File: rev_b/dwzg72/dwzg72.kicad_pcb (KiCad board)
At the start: 2 copper layers, 285 x 94.6 mm, 305 parts, among them J1 USB_B_Micro, J2 ISP, Q1 FDS9926A, SW1 circumflex, SW10 nine, SW11 zero, SW12 eszett, SW13 accent, SW14 backspace, SW15 pos1, SW16 tab, SW17 q, SW18 w, SW19 e, SW2 one, SW20 r, SW21 t, SW22 z, SW23 u, SW24 i, SW25 o, SW26 p, SW27 ü, SW28 plus, SW29 end, SW3 two, SW30 escape, SW31 a, SW32 s, SW33 d, SW34 f, SW35 g, SW36 h, SW37 j, SW38 k, SW39 l, SW4 three, SW40 ö, SW41 ä, SW42 hash, SW43 enter, SW44 delete, SW45 lshift, SW46 smaller, SW47 y, SW48 x, SW49 c, SW5 four, SW50 v, SW51 b, SW52 n, SW53 m, SW54 comma, SW55 dot, SW56 dash, SW57 up, SW58 rshift, SW59 pageup, SW6 five, SW60 control, SW61 super, SW62 alt, SW63 func, SW64 lspace, SW65 rspace, SW66 altgr, SW67 super, SW68 control, SW69 left, SW7 six, SW70 down, SW71 right, SW72 pagedown, SW73 RESET, SW8 seven, SW9 eight, U1 ATmega32U4-MU, Y1 16MHz

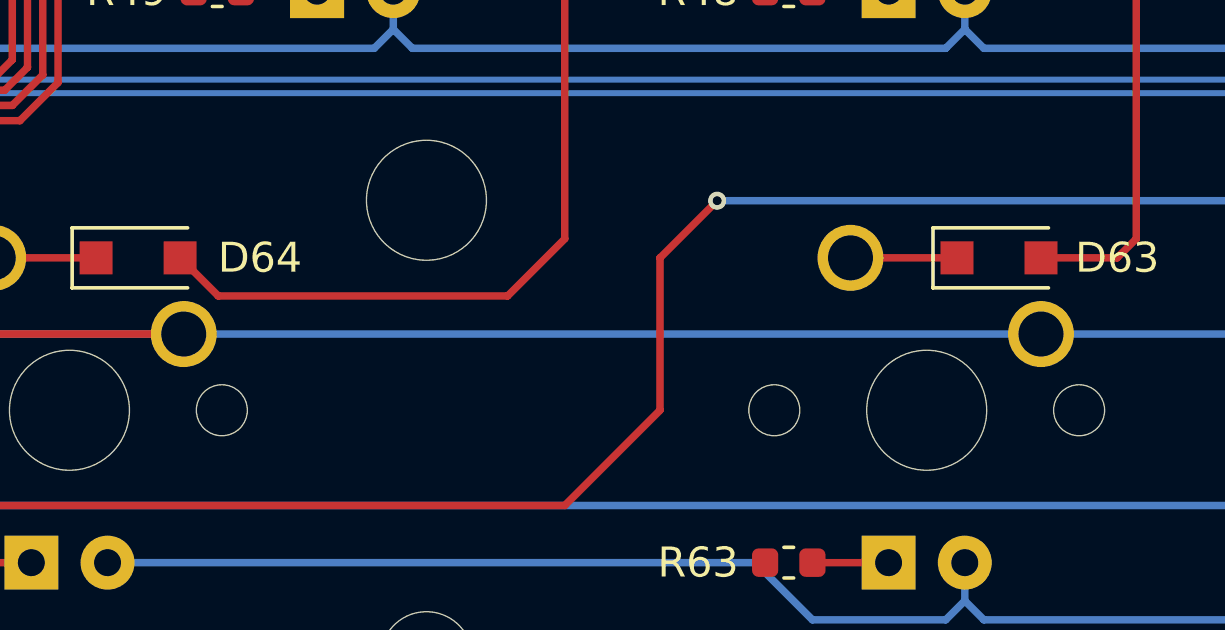
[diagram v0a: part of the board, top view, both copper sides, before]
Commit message: Add logo and revision on PCB
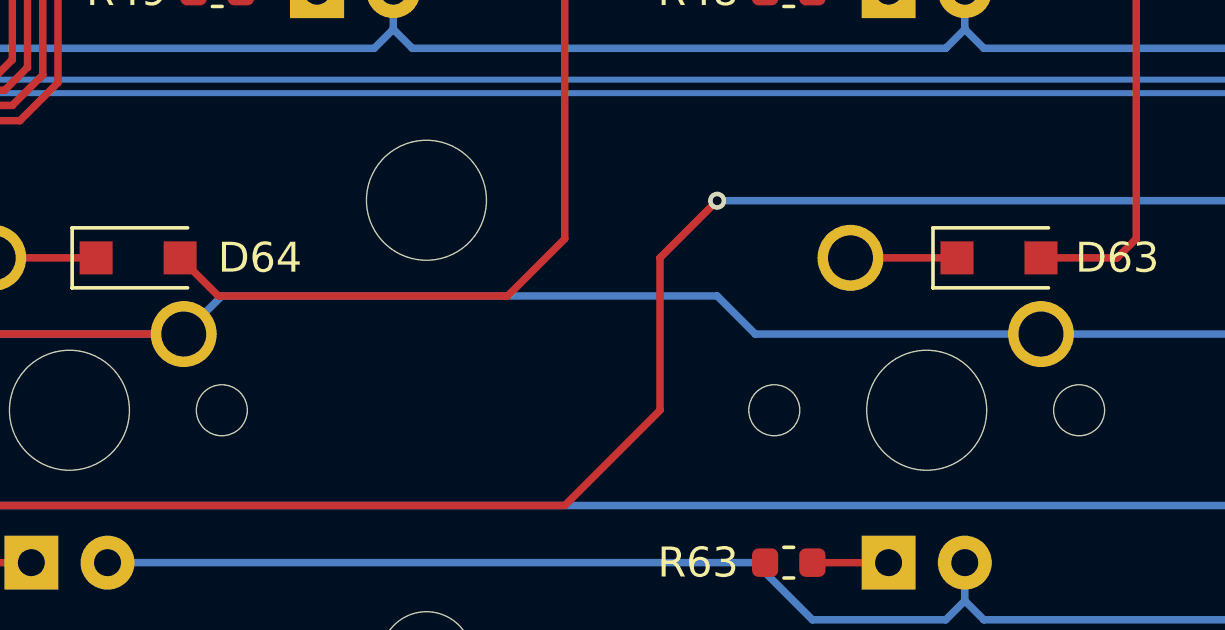
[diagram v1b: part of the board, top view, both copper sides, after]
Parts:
- added G***: LOGO, dwzg_logo:dwzg_logo_small, B.Cu at (254.1, 205.4)
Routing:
- net ROW4: track 288.7 -> 289.8 mm
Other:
- board text added: "rev b"
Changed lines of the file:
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@@
   (general
     (thickness 1.6)
-    (drawings 8)
-    (tracks 1261)
+    (drawings 9)
+    (tracks 1264)
     (zones 0)
-    (modules 305)
+    (modules 306)
     (nets 184)
   )
@@
     (add_net GND)
   )
+  (module dwzg_logo:dwzg_logo_small (layer B.Cu)
+    (at 254.085 205.38 180)
+    (fp_text reference G*** (at 0 0) (layer B.SilkS) hide
+      (effects (font (size 1.524 1.524) (thickness 0.3)) (justify mirror))
+    )
+    (fp_text value LOGO (at 0.75 0) (layer B.SilkS) hide
+      (effects (font (size 1.524 1.524) (thickness 0.3)) (justify mirror))
+    )
+    (fp_poly (pts (xy -2.73304 -0.38608) (xy -1.95072 -0.38608) (xy -1.95072 1.1684) (xy -1.1684 1.1684)
+      (xy -1.1684 -0.38608) (xy -0.38608 -0.38608) (xy -0.38608 1.1684) (xy 1.95072 1.1684)
+      (xy 1.95072 -0.38608) (xy 2.73304 -0.38608) (xy 2.73304 0.38608) (xy 3.51536 0.38608)
+      (xy 3.51536 -0.38608) (xy 4.29768 -0.38608) (xy 4.29768 0.38608) (xy 3.51536 0.38608)
+      (xy 2.73304 0.38608) (xy 2.73304 1.1684) (xy 5.08 1.1684) (xy 5.08 -2.73304)
+      (xy 2.73304 -2.73304) (xy 2.73304 -1.95072) (xy 4.29768 -1.95072) (xy 4.29768 -1.1684)
+      (xy 1.1684 -1.1684) (xy 1.1684 0.38608) (xy 0.39624 0.38608) (xy 0.39624 -1.1684)
+      (xy -5.08 -1.1684) (xy -5.08 0.38608) (xy -4.29768 0.38608) (xy -4.29768 -0.38608)
+      (xy -3.51536 -0.38608) (xy -3.51536 0.38608) (xy -4.29768 0.38608) (xy -5.08 0.38608)
+      (xy -5.08 1.1684) (xy -3.51536 1.1684) (xy -3.51536 2.73304) (xy -2.73304 2.73304)
+      (xy -2.73304 -0.38608)) (layer B.Mask) (width 0.01))
+  )
   (module Button_Switch_Keyboard:SW_Cherry_MX_1.00u_PCB (layer B.Cu)
     (at 209 124.1 180)
@@
       (effects (font (size 1 1) (thickness 0.15)) (justify mirror))
     )
-    (fp_text user %R (at -2.54 2.794) (layer B.Fab)
-      (effects (font (size 1 1) (thickness 0.15)) (justify mirror))
-    )
     (fp_line (start -8.89 1.27) (end 3.81 1.27) (layer B.Fab) (width 0.1))
     (fp_line (start 3.81 1.27) (end 3.81 -11.43) (layer B.Fab) (width 0.1))
@@
     (fp_line (start 4.445 -12.065) (end -9.525 -12.065) (layer B.SilkS) (width 0.12))
     (fp_line (start -9.525 -12.065) (end -9.525 1.905) (layer B.SilkS) (width 0.12))
+    (fp_text user %R (at -2.54 2.794) (layer B.Fab)
+      (effects (font (size 1 1) (thickness 0.15)) (justify mirror))
+    )
     (pad 1 thru_hole circle (at 0 0 180) (size 2.2 2.2) (drill 1.5) (layers *.Cu *.Mask)
       (net 68 "Net-(D65-Pad1)"))
@@
     )
   )
+  (gr_text "rev b" (at 254.085 205.38) (layer F.Mask)
+    (effects (font (size 1.5 1.5) (thickness 0.3)))
+  )
   (gr_line (start 335 211.6) (end 335 123) (layer Edge.Cuts) (width 0.05))
   (gr_line (start 50 123) (end 50 211.6) (layer Edge.Cuts) (width 0.05))
@@
   (segment (start 310.6 202.84) (end 291.55 202.84) (width 0.25) (layer B.Cu) (net 183))
   (segment (start 291.55 202.84) (end 272.5 202.84) (width 0.25) (layer B.Cu) (net 183))
-  (segment (start 272.5 202.84) (end 243.925 202.84) (width 0.25) (layer B.Cu) (net 183))
   (segment (start 205.825 202.84) (end 177.25 202.84) (width 0.25) (layer B.Cu) (net 183))
   (segment (start 177.25 202.84) (end 158.2 202.84) (width 0.25) (layer B.Cu) (net 183))
@@
   (segment (start 222.97 201.57) (end 224.24 202.84) (width 0.25) (layer B.Cu) (net 183))
   (segment (start 224.24 202.84) (end 243.925 202.84) (width 0.25) (layer B.Cu) (net 183))
+  (segment (start 243.925 202.84) (end 245.195 201.57) (width 0.25) (layer B.Cu) (net 183))
+  (segment (start 245.195 201.57) (end 261.705 201.57) (width 0.25) (layer B.Cu) (net 183))
+  (segment (start 261.705 201.57) (end 262.975 202.84) (width 0.25) (layer B.Cu) (net 183))
+  (segment (start 262.975 202.84) (end 272.5 202.84) (width 0.25) (layer B.Cu) (net 183))
   (zone (net 2) (net_name GND) (layer F.Cu) (hatch edge 0.508)
     (connect_pads (clearance 0.2))
